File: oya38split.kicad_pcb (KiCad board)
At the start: 2 copper layers, 216.7 x 104.8 mm, 89 parts, among them U1 ProMicro

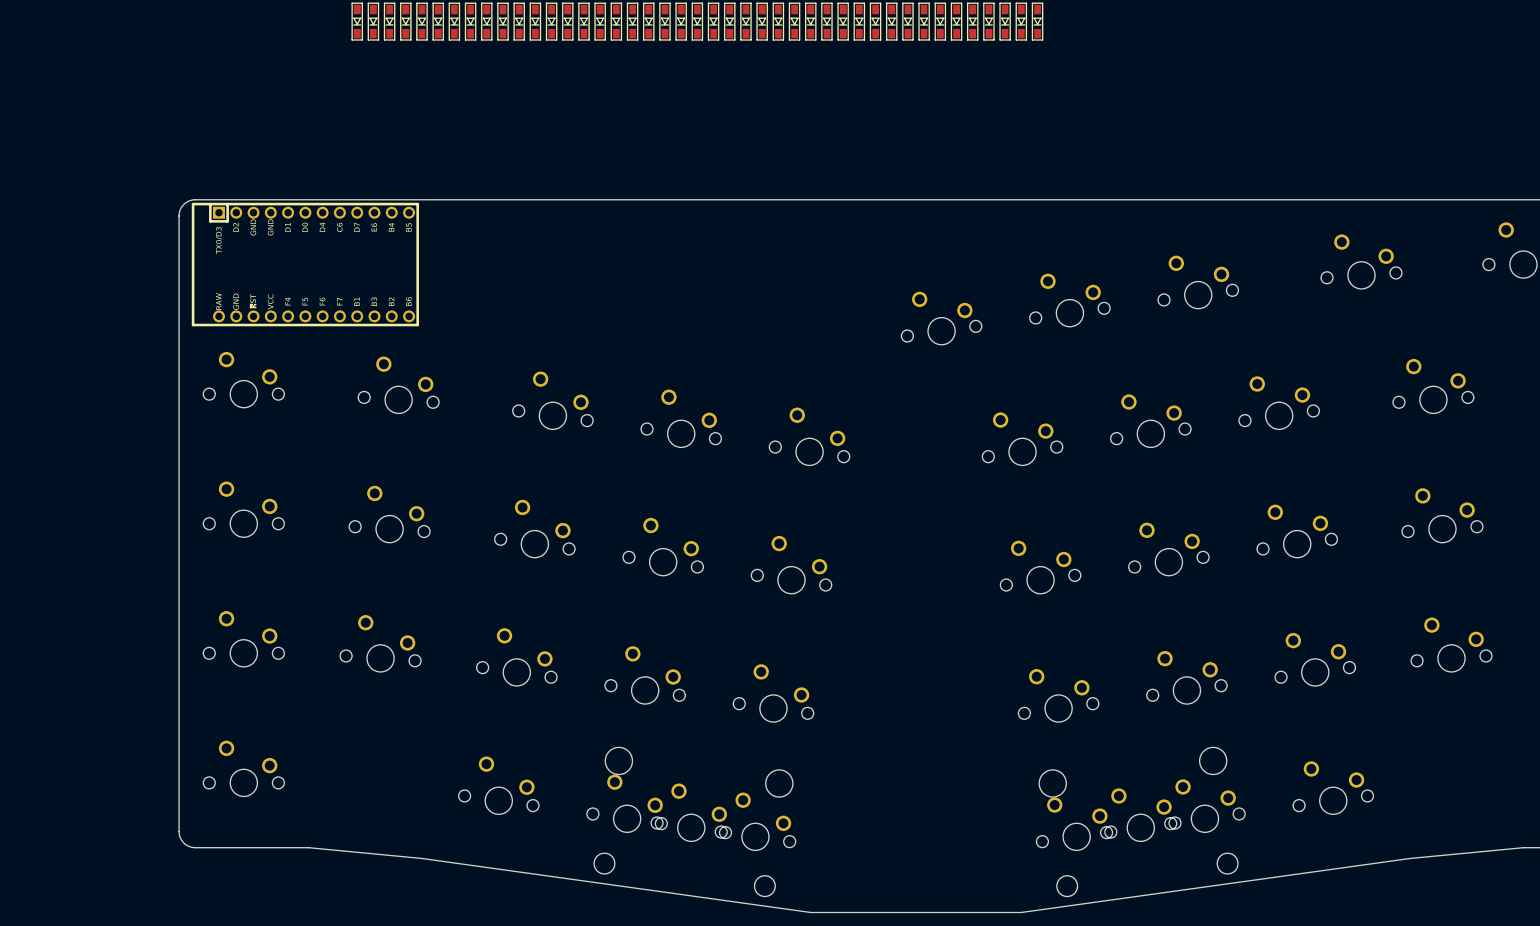
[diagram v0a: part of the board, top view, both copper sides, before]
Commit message: fixed diodes with normal layout
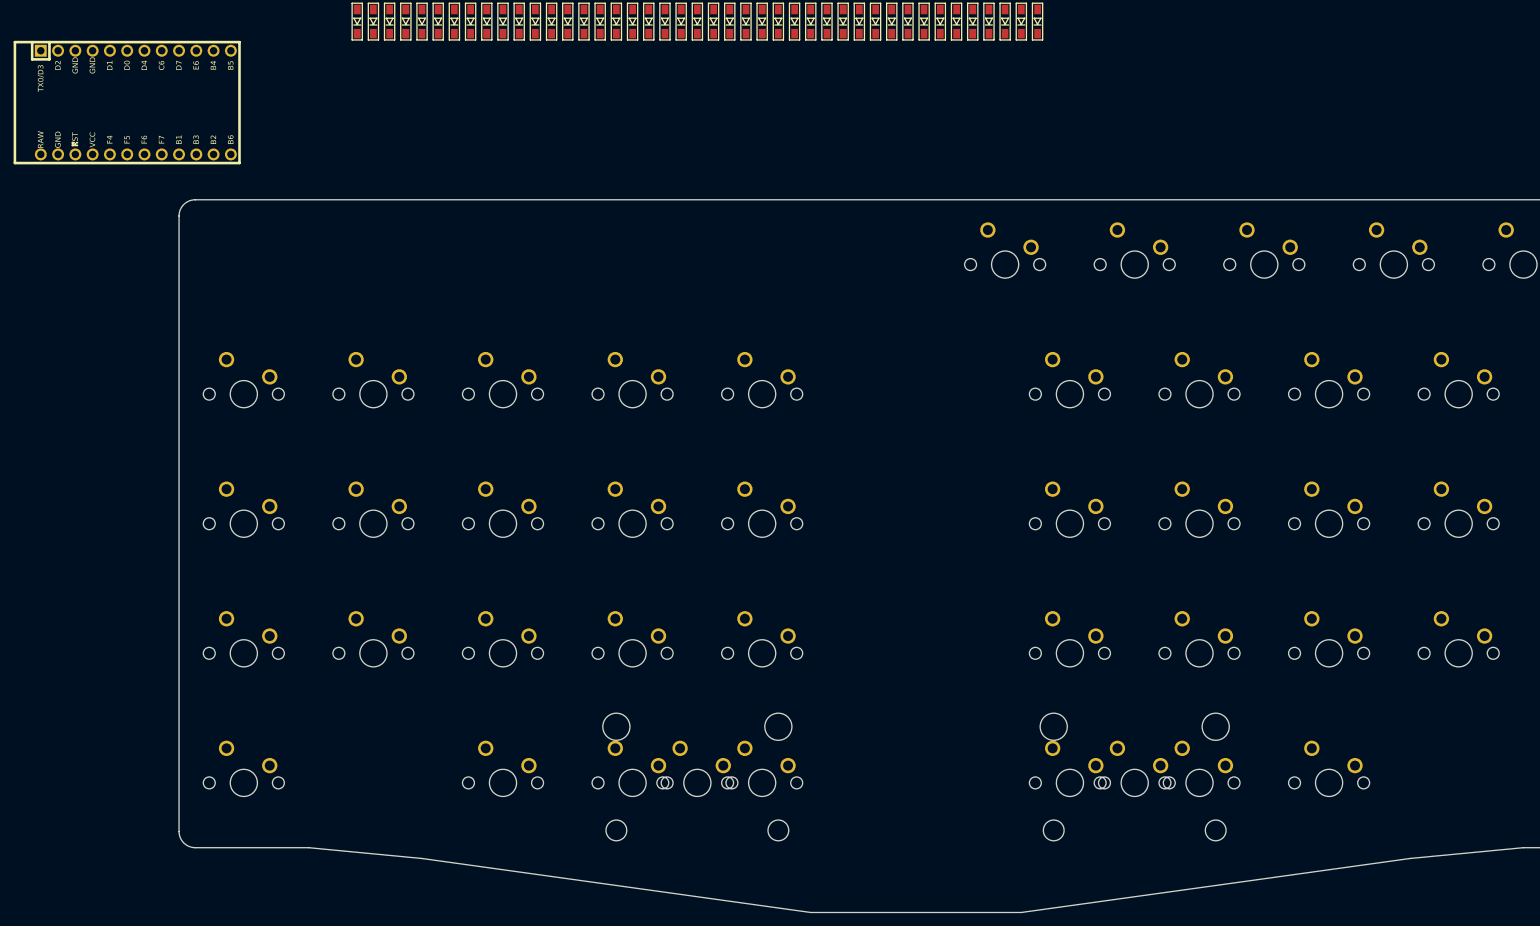
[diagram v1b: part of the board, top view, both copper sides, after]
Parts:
- moved U1 35.4 mm to (41.3, 14.3)
- moved MX39 13.5 mm to (169.1, 38.1), turned to 180 degrees
- moved MX40 11.9 mm to (188.1, 38.1), turned to 180 degrees
- moved MX5 11.0 mm to (133.3, 57.1), turned to 180 degrees
- moved MX6 11.0 mm to (178.6, 57.1), turned to 180 degrees
- moved MX41 10.7 mm to (207.2, 38.1), turned to 180 degrees
- moved MX15 9.35 mm to (133.3, 76.2), turned to 180 degrees
- moved MX16 9.35 mm to (178.6, 76.2), turned to 180 degrees
- moved MX4 9.23 mm to (114.3, 57.1), turned to 180 degrees
- moved MX7 9.23 mm to (197.6, 57.1), turned to 180 degrees
- moved MX25 8.28 mm to (133.3, 95.2), turned to 180 degrees
- moved MX26 8.28 mm to (178.6, 95.2), turned to 180 degrees
- moved MX3 8.00 mm to (95.2, 57.1), turned to 180 degrees
- moved MX8 8.00 mm to (216.7, 57.1), turned to 180 degrees
- moved MX34 7.99 mm to (133.3, 114.3), turned to 180 degrees
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
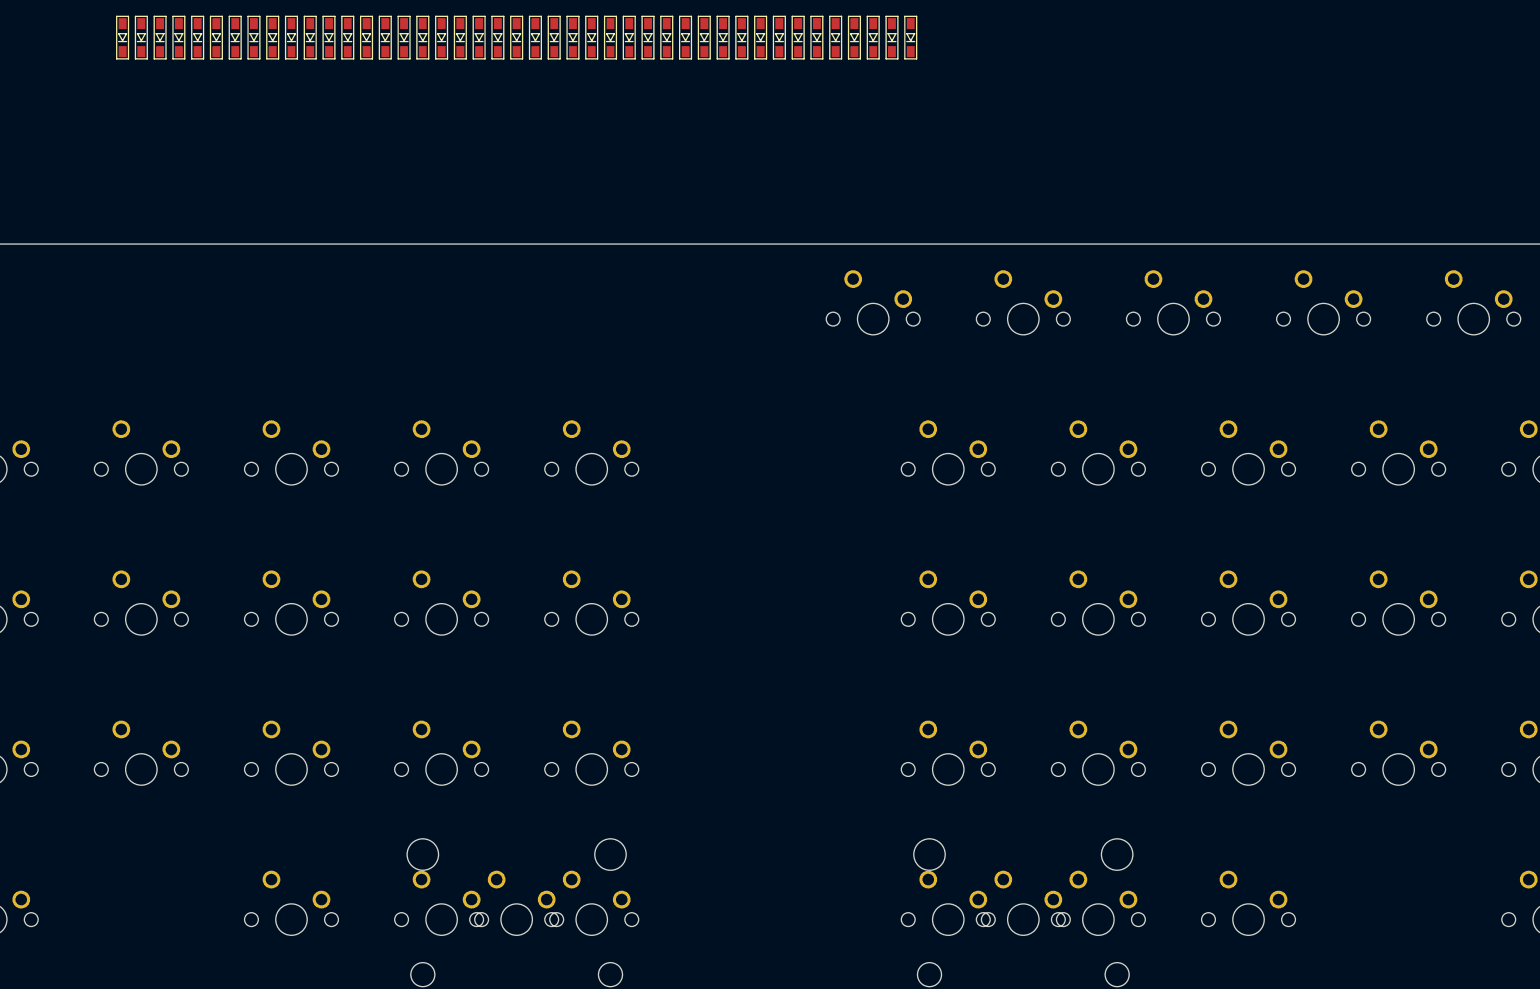
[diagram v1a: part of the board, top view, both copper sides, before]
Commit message: places diodes with switches
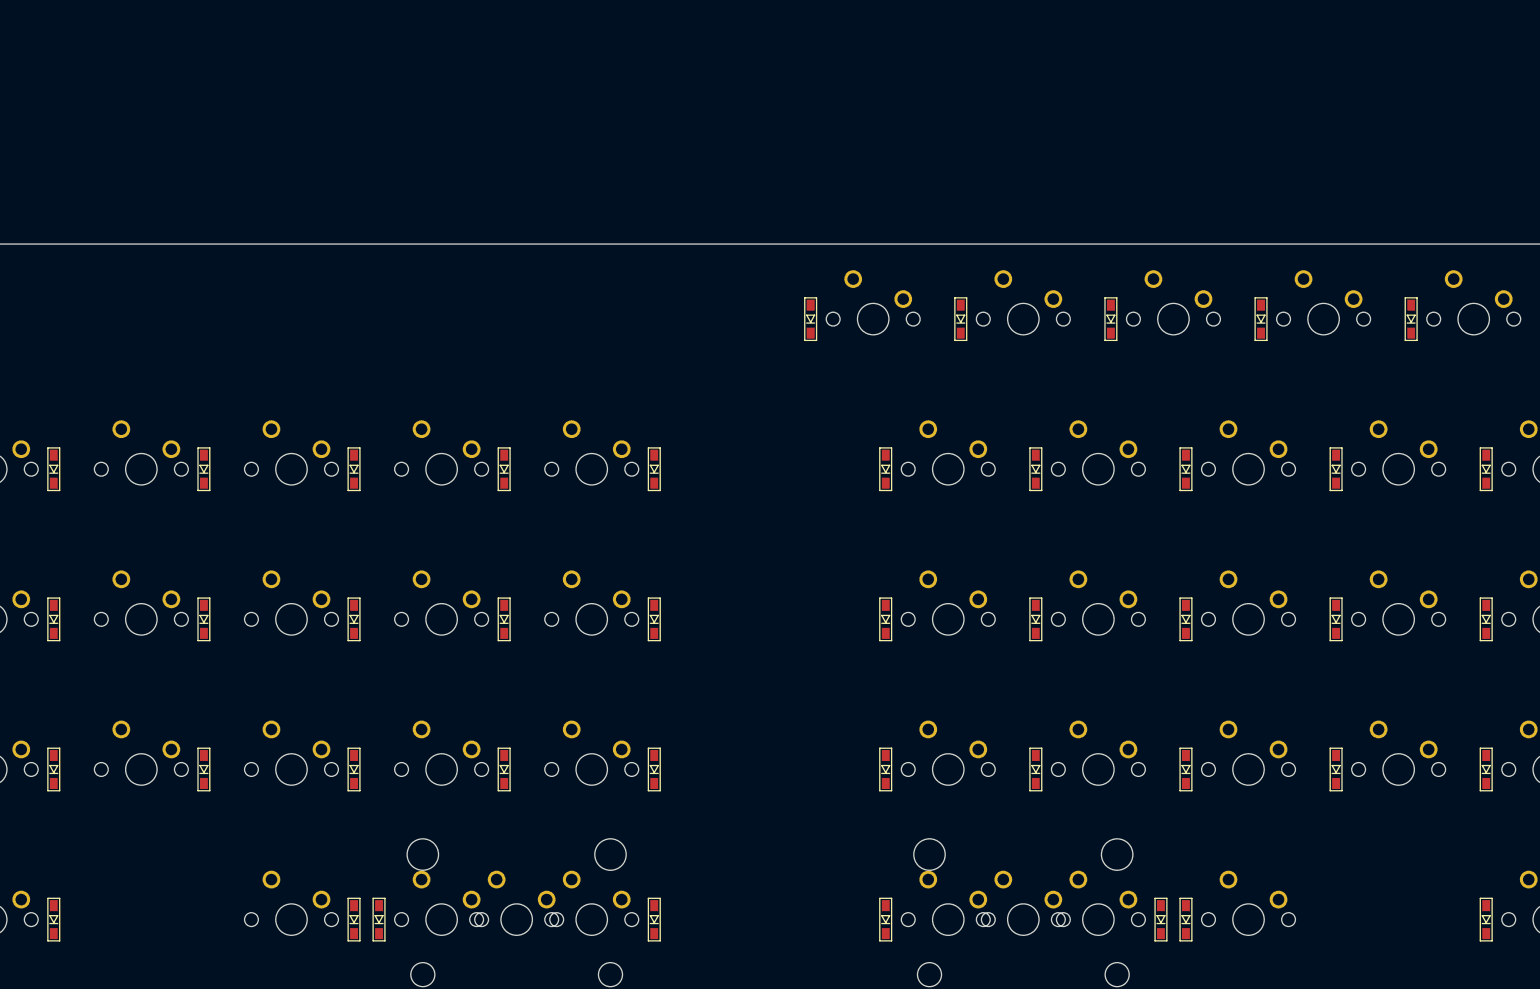
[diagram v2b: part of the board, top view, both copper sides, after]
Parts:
- moved D10 161.2 mm to (246.9, 57.1)
- moved D20 147.6 mm to (246.9, 76.2)
- moved D9 145.6 mm to (227.8, 57.1)
- moved D38 140.5 mm to (246.9, 114.3)
- moved D30 139.4 mm to (246.9, 95.2)
- moved D31 137.7 mm to (65.1, 114.3)
- moved D19 133.4 mm to (227.8, 76.2)
- moved D8 130.3 mm to (208.8, 57.1)
- moved D29 127.5 mm to (227.8, 95.2)
- moved D37 122.3 mm to (208.8, 114.3)
- moved D36 121.9 mm to (205.6, 114.3)
- moved D32 120.4 mm to (103.2, 114.3)
- moved D33 120.1 mm to (106.4, 114.3)
- moved D18 119.9 mm to (208.8, 76.2)
- moved D28 116.7 mm to (208.8, 95.2)
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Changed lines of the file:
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@@
   )
   (module kbd:D3_SMD_v2 (layer F.Cu)
-    (at 173.83125 2.38125 90)
+    (at 237.33125 38.1 90)
     (descr "Resitance 3 pas")
     (tags R)
@@
   )
   (module kbd:D3_SMD_v2 (layer F.Cu)
-    (at 171.45 2.38125 90)
+    (at 218.28125 38.1 90)
     (descr "Resitance 3 pas")
     (tags R)
@@
   )
   (module kbd:D3_SMD_v2 (layer F.Cu)
-    (at 169.06875 2.38125 90)
+    (at 199.23125 38.1 90)
     (descr "Resitance 3 pas")
     (tags R)
@@
   )
   (module kbd:D3_SMD_v2 (layer F.Cu)
-    (at 166.6875 2.38125 90)
+    (at 180.18125 38.1 90)
     (descr "Resitance 3 pas")
     (tags R)
@@
   )
   (module kbd:D3_SMD_v2 (layer F.Cu)
-    (at 164.30625 2.38125 90)
+    (at 161.13125 38.1 90)
     (descr "Resitance 3 pas")
     (tags R)
@@
   )
   (module kbd:D3_SMD_v2 (layer F.Cu)
-    (at 161.925 2.38125 90)
+    (at 246.85625 114.3 90)
     (descr "Resitance 3 pas")
     (tags R)
@@
   )
   (module kbd:D3_SMD_v2 (layer F.Cu)
-    (at 159.54375 2.38125 90)
+    (at 208.75625 114.3 90)
     (descr "Resitance 3 pas")
     (tags R)
@@
   )
   (module kbd:D3_SMD_v2 (layer F.Cu)
-    (at 157.1625 2.38125 90)
+    (at 205.58125 114.3 90)
     (descr "Resitance 3 pas")
     (tags R)
@@
   )
   (module kbd:D3_SMD_v2 (layer F.Cu)
-    (at 154.78125 2.38125 90)
+    (at 170.65625 114.3 90)
     (descr "Resitance 3 pas")
     (tags R)
@@
   )
   (module kbd:D3_SMD_v2 (layer F.Cu)
-    (at 152.4 2.38125 90)
+    (at 141.2875 114.3 90)
     (descr "Resitance 3 pas")
     (tags R)
@@
   )
   (module kbd:D3_SMD_v2 (layer F.Cu)
-    (at 150.01875 2.38125 90)
+    (at 106.3625 114.3 90)
     (descr "Resitance 3 pas")
     (tags R)
@@
   )
   (module kbd:D3_SMD_v2 (layer F.Cu)
-    (at 147.6375 2.38125 90)
+    (at 103.1875 114.3 90)
     (descr "Resitance 3 pas")
     (tags R)
@@
   )
   (module kbd:D3_SMD_v2 (layer F.Cu)
-    (at 145.25625 2.38125 90)
+    (at 65.0875 114.3 90)
     (descr "Resitance 3 pas")
     (tags R)
@@
   )
   (module kbd:D3_SMD_v2 (layer F.Cu)
-    (at 142.875 2.38125 90)
+    (at 246.85625 95.25 90)
     (descr "Resitance 3 pas")
     (tags R)
@@
   )
   (module kbd:D3_SMD_v2 (layer F.Cu)
-    (at 140.49375 2.38125 90)
+    (at 227.80625 95.25 90)
     (descr "Resitance 3 pas")
     (tags R)
@@
   )
   (module kbd:D3_SMD_v2 (layer F.Cu)
-    (at 138.1125 2.38125 90)
+    (at 208.75625 95.25 90)
     (descr "Resitance 3 pas")
     (tags R)
@@
   )
   (module kbd:D3_SMD_v2 (layer F.Cu)
-    (at 135.73125 2.38125 90)
+    (at 189.70625 95.25 90)
     (descr "Resitance 3 pas")
     (tags R)
@@
   )
   (module kbd:D3_SMD_v2 (layer F.Cu)
-    (at 133.35 2.38125 90)
+    (at 170.65625 95.25 90)
     (descr "Resitance 3 pas")
     (tags R)
@@
   )
   (module kbd:D3_SMD_v2 (layer F.Cu)
-    (at 130.96875 2.38125 90)
+    (at 141.2875 95.25 90)
     (descr "Resitance 3 pas")
     (tags R)
@@
   )
   (module kbd:D3_SMD_v2 (layer F.Cu)
-    (at 128.5875 2.38125 90)
+    (at 122.2375 95.25 90)
     (descr "Resitance 3 pas")
     (tags R)
@@
   )
   (module kbd:D3_SMD_v2 (layer F.Cu)
-    (at 126.20625 2.38125 90)
+    (at 103.1875 95.25 90)
     (descr "Resitance 3 pas")
     (tags R)
@@
   )
   (module kbd:D3_SMD_v2 (layer F.Cu)
-    (at 123.825 2.38125 90)
+    (at 84.1375 95.25 90)
     (descr "Resitance 3 pas")
     (tags R)
@@
   )
   (module kbd:D3_SMD_v2 (layer F.Cu)
-    (at 121.44375 2.38125 90)
+    (at 65.0875 95.25 90)
     (descr "Resitance 3 pas")
     (tags R)
@@
   )
   (module kbd:D3_SMD_v2 (layer F.Cu)
-    (at 119.0625 2.38125 90)
+    (at 246.85625 76.2 90)
     (descr "Resitance 3 pas")
     (tags R)
@@
   )
   (module kbd:D3_SMD_v2 (layer F.Cu)
-    (at 116.68125 2.38125 90)
+    (at 227.80625 76.2 90)
     (descr "Resitance 3 pas")
     (tags R)
@@
   )
   (module kbd:D3_SMD_v2 (layer F.Cu)
-    (at 114.3 2.38125 90)
+    (at 208.75625 76.2 90)
     (descr "Resitance 3 pas")
     (tags R)
@@
   )
   (module kbd:D3_SMD_v2 (layer F.Cu)
-    (at 111.91875 2.38125 90)
+    (at 189.70625 76.2 90)
     (descr "Resitance 3 pas")
     (tags R)
@@
   )
   (module kbd:D3_SMD_v2 (layer F.Cu)
-    (at 109.5375 2.38125 90)
+    (at 170.65625 76.2 90)
     (descr "Resitance 3 pas")
     (tags R)
@@
   )
   (module kbd:D3_SMD_v2 (layer F.Cu)
-    (at 107.15625 2.38125 90)
+    (at 141.2875 76.2 90)
     (descr "Resitance 3 pas")
     (tags R)
@@
   )
   (module kbd:D3_SMD_v2 (layer F.Cu)
-    (at 104.775 2.38125 90)
+    (at 122.2375 76.2 90)
     (descr "Resitance 3 pas")
     (tags R)
@@
   )
   (module kbd:D3_SMD_v2 (layer F.Cu)
-    (at 102.39375 2.38125 90)
+    (at 103.1875 76.2 90)
     (descr "Resitance 3 pas")
     (tags R)
@@
   )
   (module kbd:D3_SMD_v2 (layer F.Cu)
-    (at 100.0125 2.38125 90)
+    (at 84.1375 76.2 90)
     (descr "Resitance 3 pas")
     (tags R)
@@
   )
   (module kbd:D3_SMD_v2 (layer F.Cu)
-    (at 97.63125 2.38125 90)
+    (at 65.0875 76.2 90)
     (descr "Resitance 3 pas")
     (tags R)
@@
   )
   (module kbd:D3_SMD_v2 (layer F.Cu)
-    (at 95.25 2.38125 90)
+    (at 246.85625 57.15 90)
     (descr "Resitance 3 pas")
     (tags R)
@@
   )
   (module kbd:D3_SMD_v2 (layer F.Cu)
-    (at 92.86875 2.38125 90)
+    (at 227.80625 57.15 90)
     (descr "Resitance 3 pas")
     (tags R)
@@
   )
   (module kbd:D3_SMD_v2 (layer F.Cu)
-    (at 90.4875 2.38125 90)
+    (at 208.75625 57.15 90)
     (descr "Resitance 3 pas")
     (tags R)
@@
   )
   (module kbd:D3_SMD_v2 (layer F.Cu)
-    (at 88.10625 2.38125 90)
+    (at 189.70625 57.15 90)
     (descr "Resitance 3 pas")
     (tags R)
@@
   )
   (module kbd:D3_SMD_v2 (layer F.Cu)
-    (at 85.725 2.38125 90)
+    (at 170.65625 57.15 90)
     (descr "Resitance 3 pas")
     (tags R)
@@
   )
   (module kbd:D3_SMD_v2 (layer F.Cu)
-    (at 83.34375 2.38125 90)
+    (at 141.2875 57.15 90)
     (descr "Resitance 3 pas")
     (tags R)
@@
   )
   (module kbd:D3_SMD_v2 (layer F.Cu)
-    (at 80.9625 2.38125 90)
+    (at 122.2375 57.15 90)
     (descr "Resitance 3 pas")
     (tags R)
@@
   )
   (module kbd:D3_SMD_v2 (layer F.Cu)
-    (at 78.58125 2.38125 90)
+    (at 103.1875 57.15 90)
     (descr "Resitance 3 pas")
     (tags R)
@@
   )
   (module kbd:D3_SMD_v2 (layer F.Cu)
-    (at 76.2 2.38125 90)
+    (at 84.1375 57.15 90)
     (descr "Resitance 3 pas")
     (tags R)
@@
   )
   (module kbd:D3_SMD_v2 (layer F.Cu)
-    (at 73.81875 2.38125 90)
-    (descr "Resitance 3 pas")
-    (tags R)
+    (at 65.0875 57.15 90)
+    (descr "Resitance 3 pas")
+    (tags R)

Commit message: placed everything
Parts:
- D35: moved to B.Cu
- moved U1 35.4 mm to (67.5, 38.1)
- moved D35 31.7 mm to (140.2, 123.3), turned to 82 degrees
- moved D39 14.3 mm to (151.9, 49.0), turned to 98 degrees
- moved MX39 13.5 mm to (159.7, 47.9), turned to 188 degrees
- moved D40 12.5 mm to (170.7, 46.3), turned to 98 degrees
- moved MX40 11.9 mm to (178.6, 45.2), turned to 188 degrees
- moved D5 11.8 mm to (148.2, 66.7), turned to 82 degrees
- moved D6 11.8 mm to (163.8, 66.7), turned to 98 degrees
- moved D41 11.1 mm to (189.6, 43.7), turned to 98 degrees
- moved MX5 11.0 mm to (140.3, 65.6), turned to 172 degrees
- moved MX6 11.0 mm to (171.6, 65.6), turned to 188 degrees
- moved MX41 10.7 mm to (197.5, 42.6), turned to 188 degrees
- moved D15 10.3 mm to (145.5, 85.6), turned to 82 degrees
- moved D16 10.3 mm to (166.4, 85.6), turned to 98 degrees
- moved D4 9.91 mm to (129.3, 64.1), turned to 82 degrees
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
